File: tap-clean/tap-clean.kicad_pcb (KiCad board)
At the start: 2 copper layers, 96.5 x 68.6 mm, 25 parts, among them Q1 TIP42, U1 74HC595, U2 LM7805_TO220

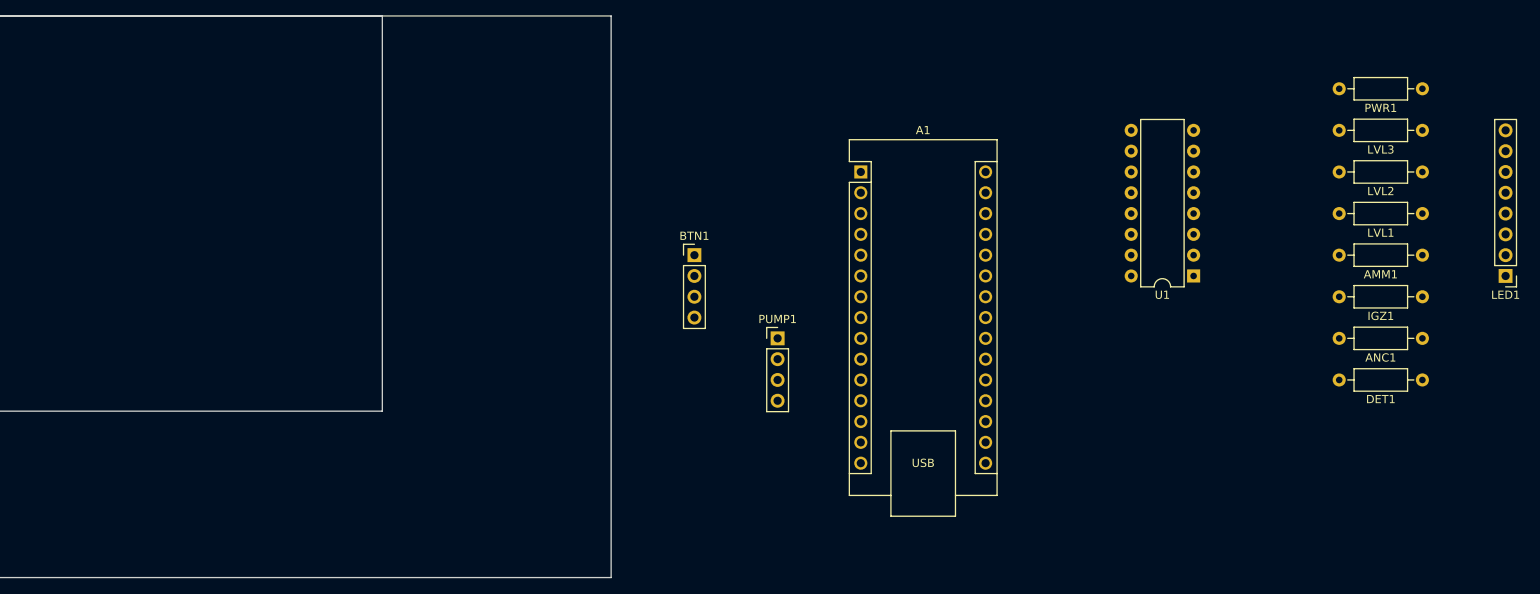
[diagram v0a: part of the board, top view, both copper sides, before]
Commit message: adding footprint to connections
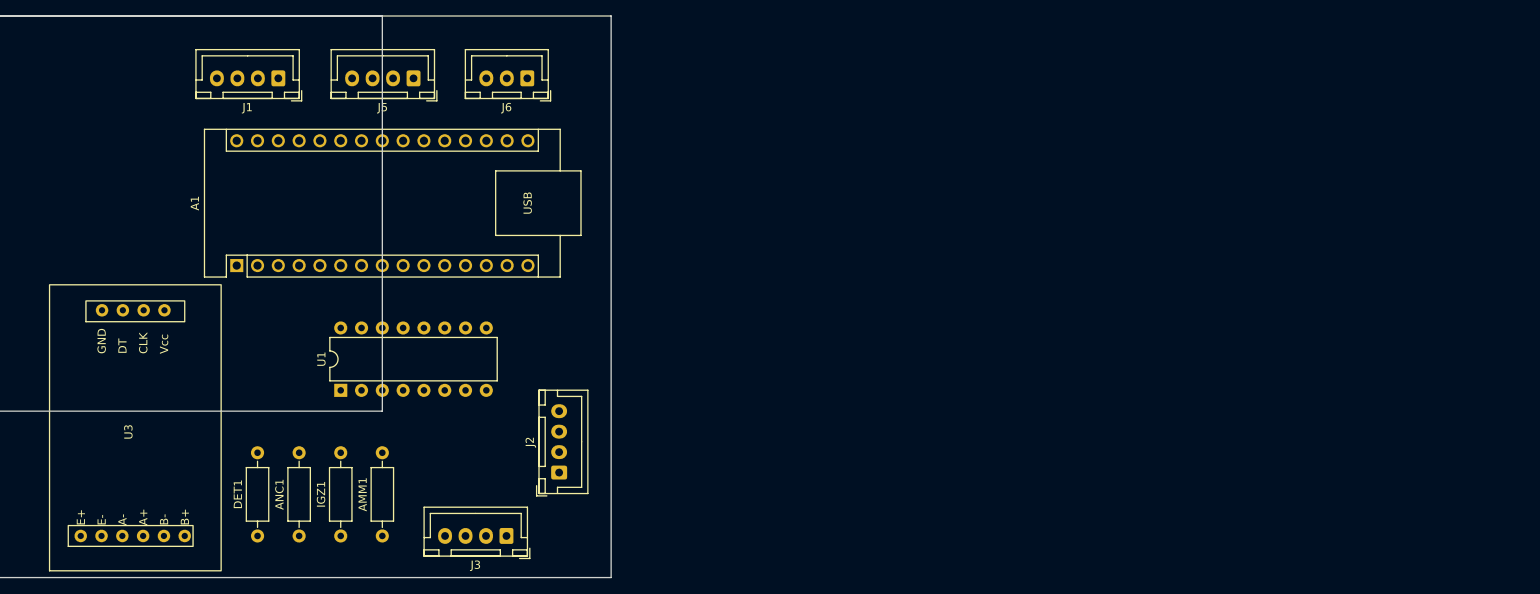
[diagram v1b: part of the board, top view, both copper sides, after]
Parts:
- removed BTN1: buttons, Connector_PinHeader_2.54mm:PinHeader_1x04_P2.54mm_Vertical
- removed LED1: Conn_01x08_Pin, Connector_PinHeader_2.54mm:PinHeader_1x08_P2.54mm_Vertical
- removed LVL1, LVL2, LVL3, PWR1: 330R, Resistor_THT:R_Axial_DIN0207_L6.3mm_D2.5mm_P10.16mm_Horizontal
- removed PUMP1: relay, Connector_PinHeader_2.54mm:PinHeader_1x04_P2.54mm_Vertical
- added J1: Stepper1, Connector_JST:JST_XH_B4B-XH-A_1x04_P2.50mm_Vertical, F.Cu at (83.8, 38.1)
- added J2: Relay, Connector_JST:JST_XH_B4B-XH-A_1x04_P2.50mm_Vertical, F.Cu at (118.1, 86.2)
- added J3: Led, Connector_JST:JST_XH_B4B-XH-A_1x04_P2.50mm_Vertical, F.Cu at (111.7, 94.0)
- added J5: LCD, Connector_JST:JST_XH_B4B-XH-A_1x04_P2.50mm_Vertical, F.Cu at (100.3, 38.1)
- added J6: CTRL, Connector_JST:JST_XH_B3B-XH-A_1x03_P2.50mm_Vertical, F.Cu at (114.2, 38.1)
- added U3: ~, dag:HX711, F.Cu at (66.0, 81.3)
- R2: value 10R -> 5R
- moved DET1 143.5 mm to (81.3, 94.0), turned to 90 degrees
- moved ANC1 139.3 mm to (86.4, 94.0), turned to 90 degrees
- moved IGZ1 135.3 mm to (91.4, 94.0), turned to 90 degrees
- moved AMM1 131.6 mm to (96.5, 94.0), turned to 90 degrees
- moved U1 105.1 mm to (91.4, 76.2), turned to 90 degrees
- moved A1 77.1 mm to (78.7, 61.0), turned to 90 degrees
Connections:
- A1 pad 10: Net-(A1-D7) -> unconnected-(A1-D7-Pad10)
- A1 pad 20: unconnected-(A1-A1-Pad20) -> Net-(A1-A1)
- A1 pad 21: unconnected-(A1-A2-Pad21) -> Net-(A1-A2)
- A1 pad 22: unconnected-(A1-A3-Pad22) -> Net-(A1-A3)
- A1 pad 25: Net-(A1-A6) -> unconnected-(A1-A6-Pad25)
- A1 pad 8: Net-(A1-D5) -> unconnected-(A1-D5-Pad8)
- A1 pad 9: Net-(A1-D6) -> unconnected-(A1-D6-Pad9)
- U1 pad 11: Net-(A1-A5) -> Net-(A1-D3)
- U1 pad 12: Net-(A1-A6) -> Net-(A1-D4)
- U1 pad 14: Net-(A1-A4) -> Net-(A1-D2)
